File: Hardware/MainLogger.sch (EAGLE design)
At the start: 203 parts, among them J3 GEMS_POWER_PLUGINPUT_RT, J4 U.FL, J5 SIM_CDNANO_SF72, Q1 DMG3404, Q2 MOSFET_PCH-DMP3036SFG, Q3 MOSFET_PCH-DMP3036SFG, Q4 DMG3404, Q5 NX2301P, Q6 NX2301P, U1 FXMAR2102UMLP, U10 SN74AUP3G34DCU, U11 SIP32431TDFN, U12 LTC4412S6, U13 TCR2LE31ESV, U14 LP59073.3VYKE, U15 MIC22602, U16 BQ25616, U17 TPS61282D, U18 MCP23018QFN, U19 MCP23018QFN, U2 VEML3328, U20 MAX-M8W, U21 MCP79412SOIC, U22 HALL_EFFECT_SI7201, U23 PCA9634QFN, U24 SN74LVC1G17DCK, U25 TPL5010DDC, U26 TPL5010DDC, U27 MB85RC, U28 FXMAR2102UMLP, U3 MMC5633, U4 MXC6655, U5 PAC1934QFN, U6 PAC1934QFN, U7 SHT40, U8 SN74AUP1G08DCK, U9 FXMAR2102UMLP

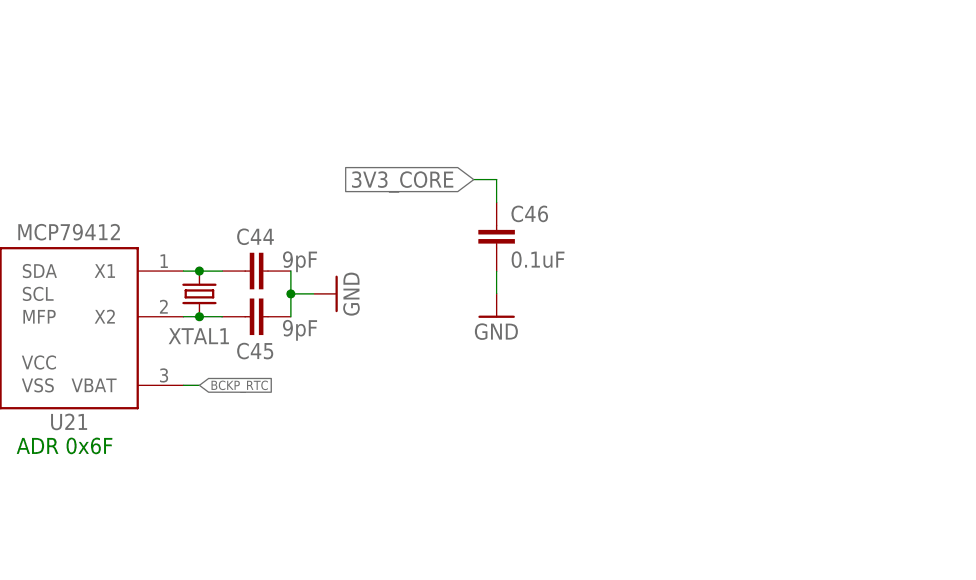
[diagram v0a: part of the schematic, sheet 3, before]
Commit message: Switched RTC crystal to TCXO
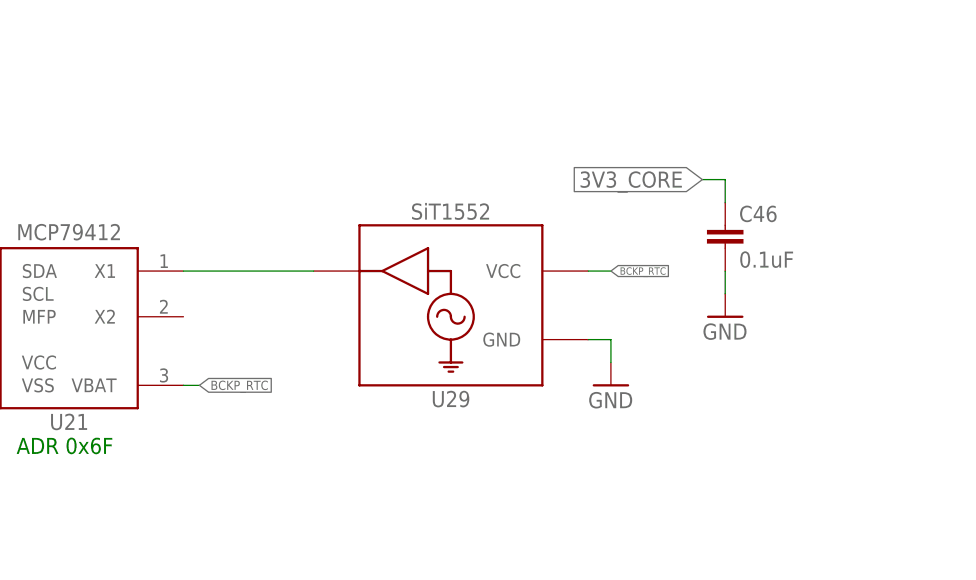
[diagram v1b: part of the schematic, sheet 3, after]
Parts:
- removed C44, C45: 9pF, bschulz_passives:C-EU9PFC0402
- removed XTAL1: CRYSTAL32.768KHZ_9PF3.2X1.5, bschulz:CRYSTAL32.768KHZ_9PF3.2X1.5
- added U29: SIT1552, bschulz:SIT1552
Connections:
- removed net N$7: C45.1, U21.X2, XTAL1.2
- net BCKP_RTC: now also U29.VCC
- net GND: now also U29.GND; no longer C44.2, C45.2
- net N$4: now also U29.CLK; no longer C44.1, XTAL1.1
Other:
- moved on the sheet: C46
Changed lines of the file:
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@@
 <part name="D4" library="bschulz" deviceset="DIODE_CC" device="SOT23" technology="BAT54C" value="BAT54C"/>
 <part name="U21" library="bschulz" deviceset="MCP794*" device="SOIC" technology="12" value="MCP79412SOIC"/>
-<part name="XTAL1" library="bschulz" deviceset="CRYSTAL" device="3.2X1.5" technology="32.768KHZ_9PF" value="CRYSTAL32.768KHZ_9PF3.2X1.5">
-<attribute name="DIGIKEY" value="535-11937-1-ND"/>
-<attribute name="MF" value="ABS07-120-32.768KHZ-T"/>
-<attribute name="MPN" value="Abracon"/>
-</part>
-<part name="C44" library="bschulz_passives" deviceset="C-EU" device="C0402" technology="9PF" value="9pF"/>
-<part name="C45" library="bschulz_passives" deviceset="C-EU" device="C0402" technology="9PF" value="9pF"/>
-<part name="GND44" library="supply1" library_urn="urn:adsk.eagle:library:371" deviceset="GND" device=""/>
 <part name="GND46" library="supply1" library_urn="urn:adsk.eagle:library:371" deviceset="GND" device=""/>
 <part name="C46" library="bschulz_passives" deviceset="C-EU" device="C0402" technology="0.1UF" value="0.1uF"/>
@@
 <part name="C52" library="bschulz_passives" deviceset="C-EU" device="C0402" technology="0.1UF" value="0.1uF"/>
 <part name="GND56" library="supply1" library_urn="urn:adsk.eagle:library:371" deviceset="GND" device=""/>
+<part name="U29" library="bschulz" deviceset="SIT1552" device=""/>
+<part name="GND44" library="supply1" library_urn="urn:adsk.eagle:library:371" deviceset="GND" device=""/>
 </parts>
 <sheets>
@@
 <attribute name="NAME" x="125.222" y="237.236" size="1.778" layer="95" ratio="15" align="center"/>
 </instance>
-<instance part="XTAL1" gate="G$1" x="139.7" y="251.46" smashed="yes" rot="R270">
-<attribute name="NAME" x="139.7" y="245.872" size="1.778" layer="95" font="vector" align="bottom-center"/>
-</instance>
-<instance part="C44" gate="G$1" x="144.78" y="254" smashed="yes" rot="R90">
-<attribute name="NAME" x="143.764" y="256.921" size="1.778" layer="95"/>
-<attribute name="VALUE" x="148.844" y="254.381" size="1.778" layer="96"/>
-</instance>
-<instance part="C45" gate="G$1" x="144.78" y="248.92" smashed="yes" rot="R90">
-<attribute name="NAME" x="143.764" y="244.221" size="1.778" layer="95"/>
-<attribute name="VALUE" x="148.844" y="246.761" size="1.778" layer="96"/>
-</instance>
-<instance part="GND44" gate="1" x="154.94" y="251.46" smashed="yes" rot="R90">
-<attribute name="VALUE" x="157.48" y="248.92" size="1.778" layer="96" rot="R90"/>
-</instance>
 <instance part="GND46" gate="1" x="109.22" y="236.22" smashed="yes">
 <attribute name="VALUE" x="106.68" y="233.68" size="1.778" layer="96"/>
 </instance>
-<instance part="C46" gate="G$1" x="172.72" y="259.08" smashed="yes">
-<attribute name="NAME" x="174.244" y="259.461" size="1.778" layer="95"/>
-<attribute name="VALUE" x="174.244" y="254.381" size="1.778" layer="96"/>
+<instance part="C46" gate="G$1" x="198.12" y="259.08" smashed="yes">
+<attribute name="NAME" x="199.644" y="259.461" size="1.778" layer="95"/>
+<attribute name="VALUE" x="199.644" y="254.381" size="1.778" layer="96"/>
 </instance>
-<instance part="GND47" gate="1" x="172.72" y="248.92" smashed="yes">
-<attribute name="VALUE" x="170.18" y="246.38" size="1.778" layer="96"/>
+<instance part="GND47" gate="1" x="198.12" y="248.92" smashed="yes">
+<attribute name="VALUE" x="195.58" y="246.38" size="1.778" layer="96"/>
 </instance>
 <instance part="R47" gate="G$1" x="91.44" y="254" smashed="yes" rot="R90">
@@
 <attribute name="VALUE" x="228.6" y="149.86" size="1.778" layer="96"/>
 </instance>
+<instance part="U29" gate="G$1" x="167.64" y="251.46" smashed="yes" rot="MR0">
+<attribute name="NAME" x="167.64" y="239.776" size="1.778" layer="95" ratio="15" rot="MR0" align="center"/>
+<attribute name="DISP" x="167.64" y="260.604" size="1.778" layer="95" ratio="15" rot="MR0" align="center"/>
+</instance>
+<instance part="GND44" gate="1" x="185.42" y="241.3" smashed="yes">
+<attribute name="VALUE" x="182.88" y="238.76" size="1.778" layer="96"/>
+</instance>
 </instances>
 <busses>
@@
 </segment>
 <segment>
-<pinref part="C44" gate="G$1" pin="2"/>
-<pinref part="C45" gate="G$1" pin="2"/>
-<wire x1="149.86" y1="254" x2="149.86" y2="251.46" width="0.1524" layer="91"/>
-<pinref part="GND44" gate="1" pin="GND"/>
-<wire x1="149.86" y1="251.46" x2="149.86" y2="248.92" width="0.1524" layer="91"/>
-<wire x1="152.4" y1="251.46" x2="149.86" y2="251.46" width="0.1524" layer="91"/>
-<junction x="149.86" y="251.46"/>
-</segment>
-<segment>
 <pinref part="U21" gate="G$1" pin="VSS"/>
 <wire x1="112.522" y1="241.3" x2="109.22" y2="241.3" width="0.1524" layer="91"/>
@@
 <segment>
 <pinref part="C46" gate="G$1" pin="2"/>
-<wire x1="172.72" y1="254" x2="172.72" y2="251.46" width="0.1524" layer="91"/>
+<wire x1="198.12" y1="254" x2="198.12" y2="251.46" width="0.1524" layer="91"/>
 <pinref part="GND47" gate="1" pin="GND"/>
 </segment>
@@
 <pinref part="GND45" gate="1" pin="GND"/>
 </segment>
+<segment>
+<pinref part="U29" gate="G$1" pin="GND"/>
+<wire x1="182.88" y1="246.38" x2="185.42" y2="246.38" width="0.1524" layer="91"/>
+<wire x1="185.42" y1="246.38" x2="185.42" y2="243.84" width="0.1524" layer="91"/>
+<pinref part="GND44" gate="1" pin="GND"/>
+</segment>
 </net>
 <net name="GPS_ANT" class="0">
@@
 </segment>
 </net>
-<net name="N$4" class="0">
-<segment>
-<pinref part="U21" gate="G$1" pin="X1"/>
-<pinref part="XTAL1" gate="G$1" pin="1"/>
-<wire x1="137.922" y1="254" x2="139.7" y2="254" width="0.1524" layer="91"/>
-<pinref part="C44" gate="G$1" pin="1"/>
-<wire x1="139.7" y1="254" x2="142.24" y2="254" width="0.1524" layer="91"/>
-<junction x="139.7" y="254"/>
-</segment>
-</net>
-<net name="N$7" class="0">
-<segment>
-<pinref part="U21" gate="G$1" pin="X2"/>
-<pinref part="XTAL1" gate="G$1" pin="2"/>
-<wire x1="137.922" y1="248.92" x2="139.7" y2="248.92" width="0.1524" layer="91"/>
-<pinref part="C45" gate="G$1" pin="1"/>
-<wire x1="139.7" y1="248.92" x2="142.24" y2="248.92" width="0.1524" layer="91"/>
-<junction x="139.7" y="248.92"/>
-</segment>
-</net>
 <net name="RTC_INT" class="0">
 <segment>
@@
 <label x="139.7" y="241.3" size="1.016" layer="95" xref="yes"/>
 </segment>
+<segment>
+<pinref part="U29" gate="G$1" pin="VCC"/>
+<wire x1="182.88" y1="254" x2="185.42" y2="254" width="0.1524" layer="91"/>
+<label x="185.42" y="254" size="0.8128" layer="95" xref="yes"/>
+</segment>
 </net>
 <net name="SDA_OB" class="0">
@@
 <segment>
 <pinref part="C46" gate="G$1" pin="1"/>
-<wire x1="172.72" y1="261.62" x2="172.72" y2="264.16" width="0.1524" layer="91"/>
-<wire x1="172.72" y1="264.16" x2="170.18" y2="264.16" width="0.1524" layer="91"/>
-<label x="170.18" y="264.16" size="1.778" layer="95" rot="R180" xref="yes"/>
+<wire x1="198.12" y1="261.62" x2="198.12" y2="264.16" width="0.1524" layer="91"/>
+<wire x1="198.12" y1="264.16" x2="195.58" y2="264.16" width="0.1524" layer="91"/>
+<label x="195.58" y="264.16" size="1.778" layer="95" rot="R180" xref="yes"/>
 </segment>
 <segment>
@@
 </segment>
 </net>
+<net name="N$4" class="0">
+<segment>
+<pinref part="U29" gate="G$1" pin="CLK"/>
+<pinref part="U21" gate="G$1" pin="X1"/>
+<wire x1="152.4" y1="254" x2="137.922" y2="254" width="0.1524" layer="91"/>
+</segment>
+</net>

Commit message: Fixed passive value, added BoM
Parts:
- R49: value (none) -> 100k
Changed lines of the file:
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@@
 <part name="J5" library="bschulz" deviceset="SIM_CD" device="NANO_SF72"/>
 <part name="U24" library="bschulz" deviceset="SN74LVC1G17" device="DCK"/>
-<part name="R49" library="bschulz_passives" deviceset="R-EU_" device="R0402" technology="100K"/>
+<part name="R49" library="bschulz_passives" deviceset="R-EU_" device="R0402" technology="100K" value="100k"/>
 <part name="GND45" library="supply1" library_urn="urn:adsk.eagle:library:371" deviceset="GND" device=""/>
 <part name="U28" library="bschulz" deviceset="FXMAR2102" device="UMLP"/>

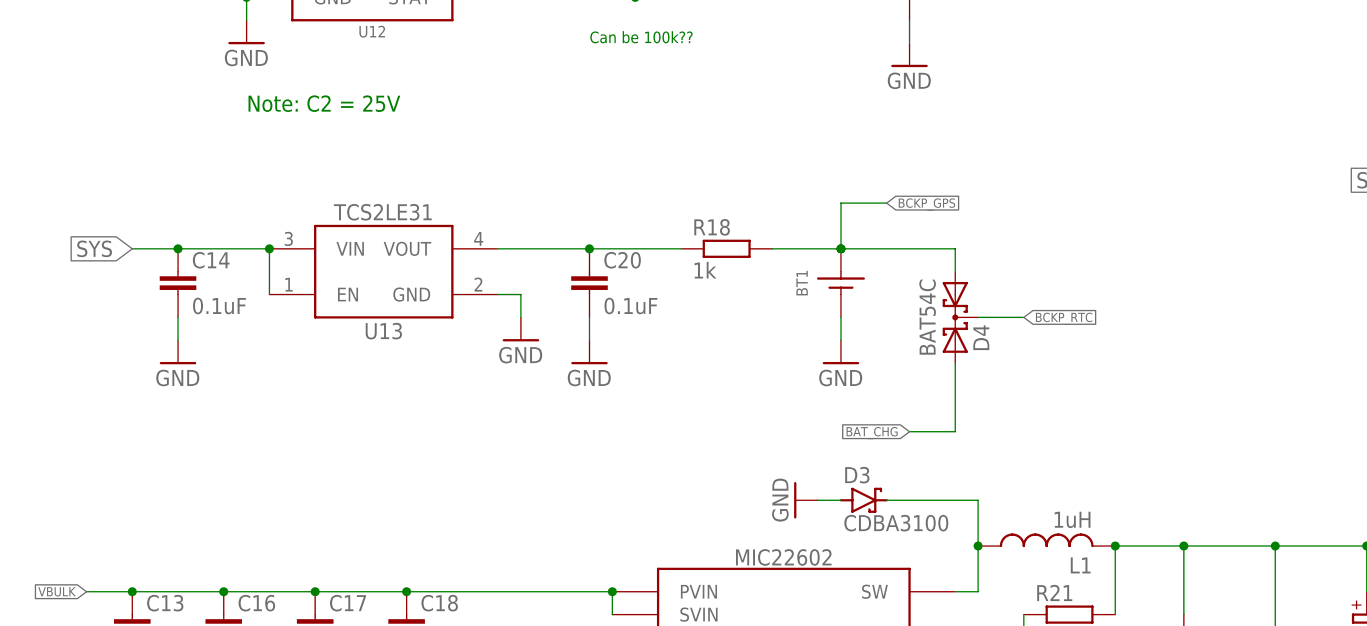
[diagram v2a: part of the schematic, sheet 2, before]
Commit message: v1.3 Updates
Reconfigured backup battery charger
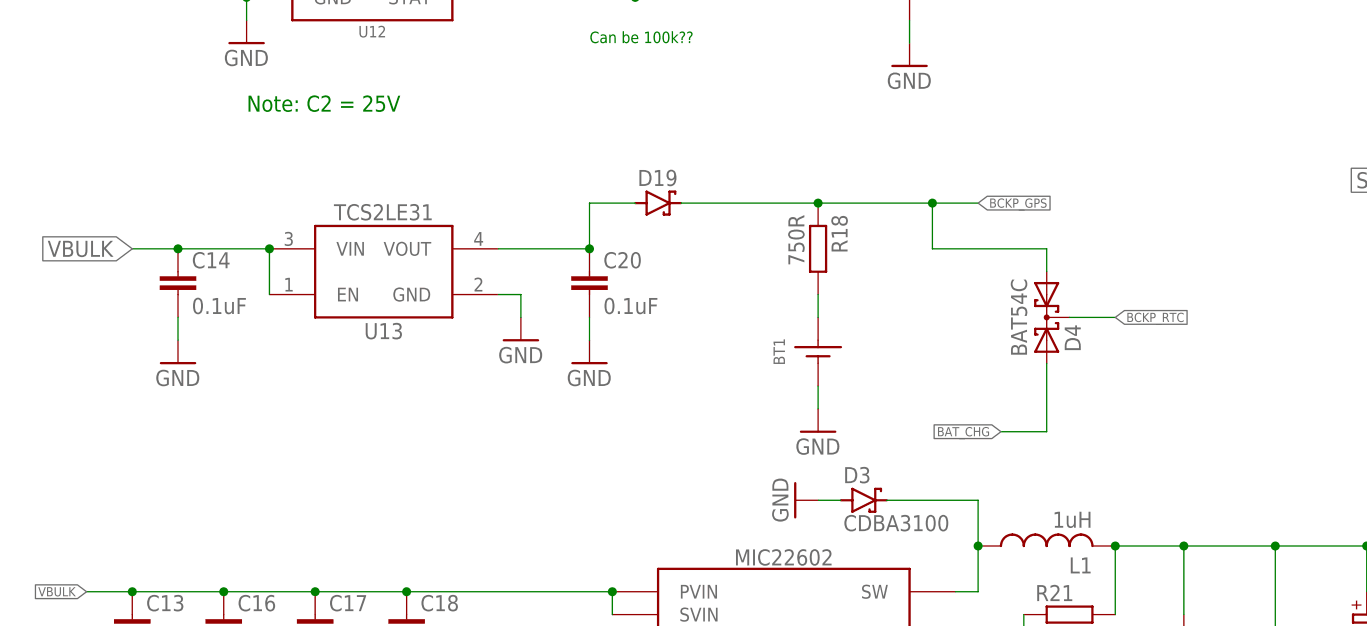
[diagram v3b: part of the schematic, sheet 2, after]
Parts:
- added D19: (no value), bschulz:DIODE_SCHOTTKYSOD-323
- R18: value 1k -> 750R
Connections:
- new net N$7: BT1.+, R18.2
- net BCKP_GPS: now also D19.C, R18.1; no longer BT1.+, R18.2
- net N$3: now also D19.A; no longer R18.1
- net SYS: no longer C14.1, U13.EN, U13.VIN
- net VBULK: now also C14.1, U13.EN, U13.VIN
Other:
- moved on the sheet: BT1, D4, R18
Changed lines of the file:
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@@
 <part name="BT1" library="bschulz" deviceset="BATTERY_COIN" device="ML621"/>
 <part name="GND30" library="supply1" library_urn="urn:adsk.eagle:library:371" deviceset="GND" device=""/>
-<part name="R18" library="bschulz_passives" deviceset="R-EU_" device="R0603" technology="1K" value="1k"/>
+<part name="R18" library="bschulz_passives" deviceset="R-EU_" device="R0603" technology="1K" value="750R"/>
 <part name="D4" library="bschulz" deviceset="DIODE_CC" device="SOT23" technology="BAT54C" value="BAT54C"/>
 <part name="U21" library="bschulz" deviceset="MCP794*" device="SOIC" technology="12" value="MCP79412SOIC"/>
@@
 <part name="U29" library="bschulz" deviceset="SIT1552" device=""/>
 <part name="GND44" library="supply1" library_urn="urn:adsk.eagle:library:371" deviceset="GND" device=""/>
+<part name="D19" library="bschulz" deviceset="DIODE_SCHOTTKY" device="SOD-323">
+<attribute name="DIGIKEY" value="BAT54WS-TPCT-ND"/>
+</part>
 </parts>
 <sheets>
@@
 <attribute name="VALUE" x="63.5" y="73.66" size="1.778" layer="96"/>
 </instance>
-<instance part="BT1" gate="G$1" x="101.6" y="81.28" smashed="yes">
-<attribute name="NAME" x="97.282" y="82.55" size="1.27" layer="95" rot="R90" align="center"/>
-</instance>
-<instance part="GND30" gate="1" x="101.6" y="73.66" smashed="yes">
-<attribute name="VALUE" x="99.06" y="71.12" size="1.778" layer="96"/>
-</instance>
-<instance part="R18" gate="G$1" x="88.9" y="86.36" smashed="yes">
-<attribute name="NAME" x="85.09" y="87.8586" size="1.778" layer="95"/>
-<attribute name="VALUE" x="85.09" y="83.058" size="1.778" layer="96"/>
-</instance>
-<instance part="D4" gate="G$1" x="114.3" y="78.74" smashed="yes" rot="R270">
-<attribute name="NAME" x="116.3066" y="77.978" size="1.778" layer="95" rot="R270"/>
-<attribute name="VALUE" x="110.3376" y="83.058" size="1.778" layer="96" rot="R270"/>
+<instance part="BT1" gate="G$1" x="99.06" y="73.66" smashed="yes">
+<attribute name="NAME" x="94.742" y="74.93" size="1.27" layer="95" rot="R90" align="center"/>
+</instance>
+<instance part="GND30" gate="1" x="99.06" y="66.04" smashed="yes">
+<attribute name="VALUE" x="96.52" y="63.5" size="1.778" layer="96"/>
+</instance>
+<instance part="R18" gate="G$1" x="99.06" y="86.36" smashed="yes" rot="R270">
+<attribute name="NAME" x="100.5586" y="90.17" size="1.778" layer="95" rot="R270"/>
+<attribute name="VALUE" x="95.758" y="90.17" size="1.778" layer="96" rot="R270"/>
+</instance>
+<instance part="D4" gate="G$1" x="124.46" y="78.74" smashed="yes" rot="R270">
+<attribute name="NAME" x="126.4666" y="77.978" size="1.778" layer="95" rot="R270"/>
+<attribute name="VALUE" x="120.4976" y="83.058" size="1.778" layer="96" rot="R270"/>
 </instance>
 <instance part="U14" gate="G$1" x="58.42" y="182.88" smashed="yes">
@@
 <attribute name="NAME" x="243.078" y="168.1734" size="1.778" layer="95" rot="R180"/>
 <attribute name="VALUE" x="248.158" y="174.1424" size="1.778" layer="96" rot="R180"/>
+</instance>
+<instance part="D19" gate="G$1" x="81.28" y="91.44" smashed="yes">
+<attribute name="NAME" x="78.994" y="93.345" size="1.778" layer="95"/>
+<attribute name="VALUE" x="78.994" y="88.011" size="1.778" layer="96"/>
 </instance>
 </instances>
@@
 <pinref part="GND30" gate="1" pin="GND"/>
 <pinref part="BT1" gate="G$1" pin="-"/>
-<wire x1="101.6" y1="76.2" x2="101.6" y2="78.74" width="0.1524" layer="91"/>
+<wire x1="99.06" y1="68.58" x2="99.06" y2="71.12" width="0.1524" layer="91"/>
 </segment>
 <segment>
@@
 <segment>
 <pinref part="D4" gate="G$1" pin="A2"/>
-<wire x1="114.3" y1="73.66" x2="114.3" y2="66.04" width="0.1524" layer="91"/>
-<wire x1="114.3" y1="66.04" x2="109.22" y2="66.04" width="0.1524" layer="91"/>
-<label x="109.22" y="66.04" size="1.016" layer="95" rot="R180" xref="yes"/>
+<wire x1="124.46" y1="73.66" x2="124.46" y2="66.04" width="0.1524" layer="91"/>
+<wire x1="124.46" y1="66.04" x2="119.38" y2="66.04" width="0.1524" layer="91"/>
+<label x="119.38" y="66.04" size="1.016" layer="95" rot="R180" xref="yes"/>
 </segment>
 </net>
@@
 </segment>
 <segment>
-<pinref part="U13" gate="G$1" pin="EN"/>
-<pinref part="U13" gate="G$1" pin="VIN"/>
-<wire x1="38.1" y1="81.28" x2="38.1" y2="86.36" width="0.1524" layer="91"/>
-<pinref part="C14" gate="G$1" pin="1"/>
-<wire x1="38.1" y1="86.36" x2="27.94" y2="86.36" width="0.1524" layer="91"/>
-<junction x="38.1" y="86.36"/>
-<wire x1="27.94" y1="86.36" x2="22.86" y2="86.36" width="0.1524" layer="91"/>
-<junction x="27.94" y="86.36"/>
-<label x="22.86" y="86.36" size="1.778" layer="95" rot="R180" xref="yes"/>
-</segment>
-<segment>
 <pinref part="U17" gate="G$1" pin="VIN"/>
 <wire x1="203.2" y1="91.44" x2="203.2" y2="88.9" width="0.1524" layer="91"/>
@@
 <pinref part="C20" gate="G$1" pin="1"/>
 <wire x1="63.5" y1="86.36" x2="73.66" y2="86.36" width="0.1524" layer="91"/>
-<wire x1="73.66" y1="86.36" x2="83.82" y2="86.36" width="0.1524" layer="91"/>
+<wire x1="73.66" y1="86.36" x2="73.66" y2="91.44" width="0.1524" layer="91"/>
 <junction x="73.66" y="86.36"/>
+<pinref part="D19" gate="G$1" pin="A"/>
+<wire x1="73.66" y1="91.44" x2="78.74" y2="91.44" width="0.1524" layer="91"/>
+</segment>
+</net>
+<net name="BCKP_GPS" class="0">
+<segment>
+<label x="116.84" y="91.44" size="1.016" layer="95" xref="yes"/>
+<pinref part="D19" gate="G$1" pin="C"/>
 <pinref part="R18" gate="G$1" pin="1"/>
-</segment>
-</net>
-<net name="BCKP_GPS" class="0">
-<segment>
-<pinref part="R18" gate="G$1" pin="2"/>
-<pinref part="BT1" gate="G$1" pin="+"/>
-<wire x1="93.98" y1="86.36" x2="101.6" y2="86.36" width="0.1524" layer="91"/>
-<junction x="101.6" y="86.36"/>
+<wire x1="83.82" y1="91.44" x2="99.06" y2="91.44" width="0.1524" layer="91"/>
+<wire x1="99.06" y1="91.44" x2="111.76" y2="91.44" width="0.1524" layer="91"/>
+<junction x="99.06" y="91.44"/>
+<wire x1="111.76" y1="91.44" x2="116.84" y2="91.44" width="0.1524" layer="91"/>
+<wire x1="111.76" y1="91.44" x2="111.76" y2="86.36" width="0.1524" layer="91"/>
+<junction x="111.76" y="91.44"/>
 <pinref part="D4" gate="G$1" pin="A1"/>
-<wire x1="101.6" y1="86.36" x2="114.3" y2="86.36" width="0.1524" layer="91"/>
-<wire x1="114.3" y1="86.36" x2="114.3" y2="83.82" width="0.1524" layer="91"/>
-<wire x1="101.6" y1="86.36" x2="101.6" y2="91.44" width="0.1524" layer="91"/>
-<junction x="101.6" y="86.36"/>
-<wire x1="101.6" y1="91.44" x2="106.68" y2="91.44" width="0.1524" layer="91"/>
-<label x="106.68" y="91.44" size="1.016" layer="95" xref="yes"/>
+<wire x1="124.46" y1="86.36" x2="124.46" y2="83.82" width="0.1524" layer="91"/>
+<wire x1="111.76" y1="86.36" x2="124.46" y2="86.36" width="0.1524" layer="91"/>
 </segment>
 </net>
@@
 <segment>
 <pinref part="D4" gate="G$1" pin="C"/>
-<wire x1="116.84" y1="78.74" x2="121.92" y2="78.74" width="0.1524" layer="91"/>
-<label x="121.92" y="78.74" size="1.016" layer="95" xref="yes"/>
+<wire x1="127" y1="78.74" x2="132.08" y2="78.74" width="0.1524" layer="91"/>
+<label x="132.08" y="78.74" size="1.016" layer="95" xref="yes"/>
 </segment>
 </net>
@@
 <label x="27.94" y="185.42" size="1.778" layer="95" rot="R180" xref="yes"/>
 </segment>
+<segment>
+<pinref part="U13" gate="G$1" pin="EN"/>
+<pinref part="U13" gate="G$1" pin="VIN"/>
+<wire x1="38.1" y1="81.28" x2="38.1" y2="86.36" width="0.1524" layer="91"/>
+<pinref part="C14" gate="G$1" pin="1"/>
+<wire x1="38.1" y1="86.36" x2="27.94" y2="86.36" width="0.1524" layer="91"/>
+<junction x="38.1" y="86.36"/>
+<wire x1="27.94" y1="86.36" x2="22.86" y2="86.36" width="0.1524" layer="91"/>
+<junction x="27.94" y="86.36"/>
+<label x="22.86" y="86.36" size="1.778" layer="95" rot="R180" xref="yes"/>
+</segment>
 </net>
 <net name="3V3_BULK+" class="0">
@@
 </segment>
 </net>
+<net name="N$7" class="0">
+<segment>
+<pinref part="BT1" gate="G$1" pin="+"/>
+<pinref part="R18" gate="G$1" pin="2"/>
+<wire x1="99.06" y1="78.74" x2="99.06" y2="81.28" width="0.1524" layer="91"/>
+</segment>
+</net>
